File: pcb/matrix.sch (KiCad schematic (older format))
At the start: 143 parts

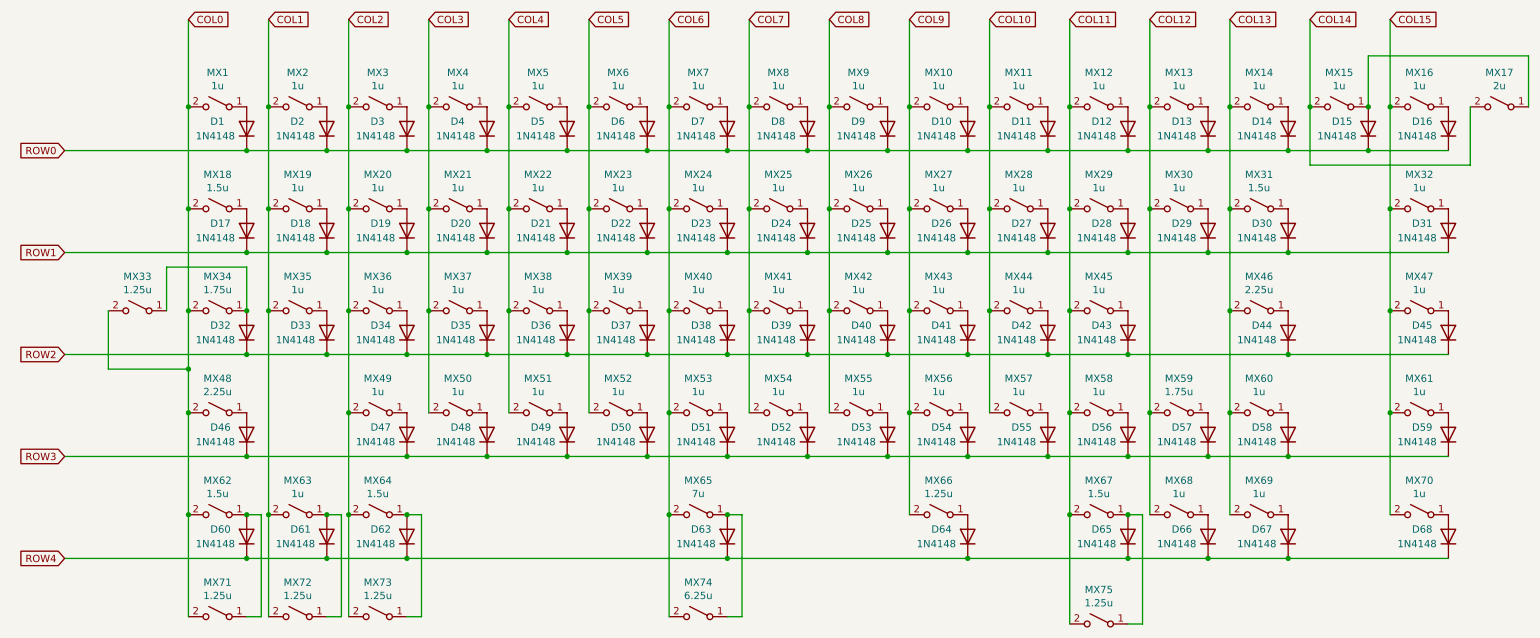
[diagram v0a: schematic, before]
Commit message: ソケットに対応。
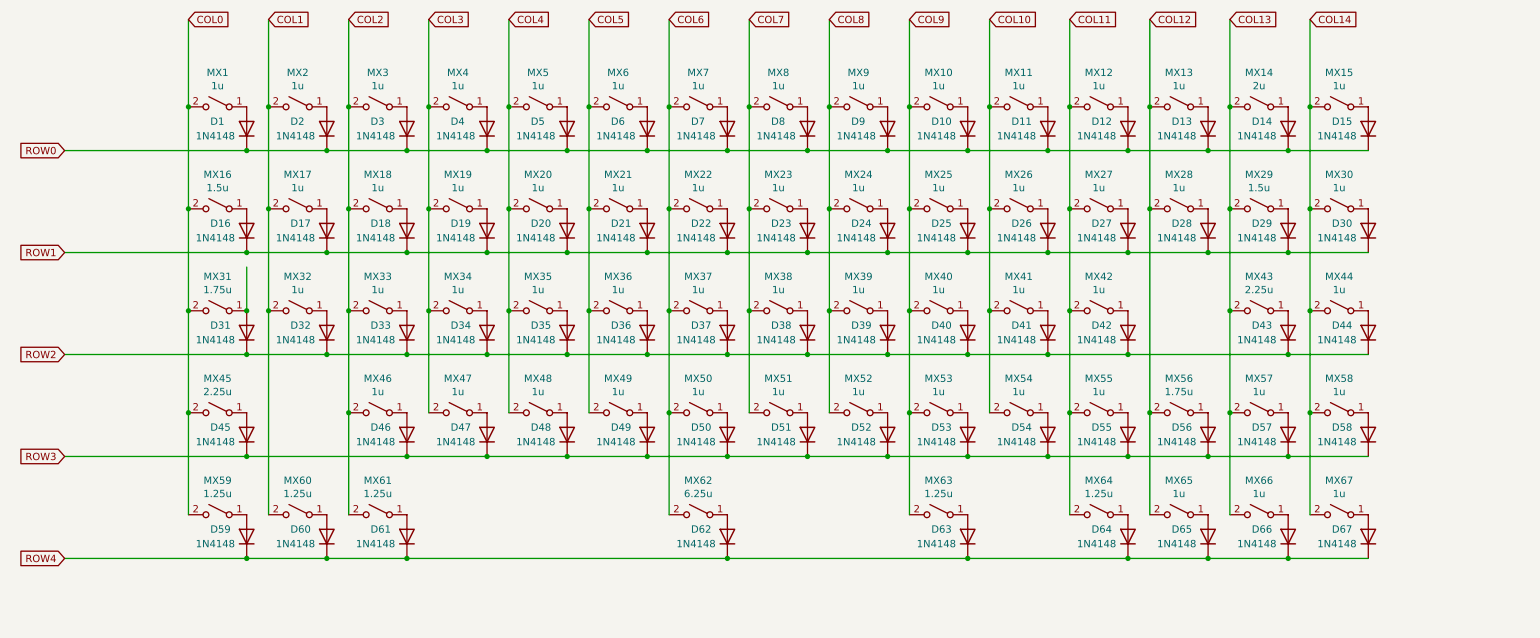
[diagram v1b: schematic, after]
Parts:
- removed D14: 1N4148, Diode_SMD:D_SOD-123, symbol Device:D
- removed MX14, MX15, MX63: 1u, MX_Only:MXOnly-1U-NoLED, symbol Switch:SW_SPST
- removed MX33: 1.25u, MX_Only:MXOnly-1.25U-NoLED, symbol Switch:SW_SPST
- removed MX62, MX64, MX67: 1.5u, MX_Only:MXOnly-1.5U-NoLED, symbol Switch:SW_SPST
- removed MX65: 7u, MX_Only:MXOnly-7U-ReversedStabilizers-NoLED, symbol Switch:SW_SPST
- MX1, MX10, MX11, MX12, MX13, MX2, MX3, MX4, MX5, MX6, MX7, MX8, MX9: footprint MX_Only:MXOnly-1U-NoLED -> MX_Only:MXOnly-1U-Hotswap
- MX14: renamed from MX17; footprint MX_Only:MXOnly-2U-NoLED -> MX_Only:MXOnly-2U-Hotswap
- MX15: renamed from MX16; footprint MX_Only:MXOnly-1U-NoLED -> MX_Only:MXOnly-1U-Hotswap
- MX16: renamed from MX18; footprint MX_Only:MXOnly-1.5U-NoLED -> MX_Only:MXOnly-1.5U-Hotswap
- MX17: renamed from MX19; footprint MX_Only:MXOnly-1U-NoLED -> MX_Only:MXOnly-1U-Hotswap
- MX18: renamed from MX20; footprint MX_Only:MXOnly-1U-NoLED -> MX_Only:MXOnly-1U-Hotswap
- MX19: renamed from MX21; footprint MX_Only:MXOnly-1U-NoLED -> MX_Only:MXOnly-1U-Hotswap
- MX20: renamed from MX22; footprint MX_Only:MXOnly-1U-NoLED -> MX_Only:MXOnly-1U-Hotswap
- MX21: renamed from MX23; footprint MX_Only:MXOnly-1U-NoLED -> MX_Only:MXOnly-1U-Hotswap
- MX22: renamed from MX24; footprint MX_Only:MXOnly-1U-NoLED -> MX_Only:MXOnly-1U-Hotswap
- MX23: renamed from MX25; footprint MX_Only:MXOnly-1U-NoLED -> MX_Only:MXOnly-1U-Hotswap
- MX24: renamed from MX26; footprint MX_Only:MXOnly-1U-NoLED -> MX_Only:MXOnly-1U-Hotswap
- MX25: renamed from MX27; footprint MX_Only:MXOnly-1U-NoLED -> MX_Only:MXOnly-1U-Hotswap
- MX26: renamed from MX28; footprint MX_Only:MXOnly-1U-NoLED -> MX_Only:MXOnly-1U-Hotswap
- MX27: renamed from MX29; footprint MX_Only:MXOnly-1U-NoLED -> MX_Only:MXOnly-1U-Hotswap
- MX28: renamed from MX30; footprint MX_Only:MXOnly-1U-NoLED -> MX_Only:MXOnly-1U-Hotswap
- MX29: renamed from MX31; footprint MX_Only:MXOnly-1.5U-NoLED -> MX_Only:MXOnly-1.5U-Hotswap
- MX30: renamed from MX32; footprint MX_Only:MXOnly-1U-NoLED -> MX_Only:MXOnly-1U-Hotswap
- MX31: renamed from MX34; footprint MX_Only:MXOnly-1.75U-NoLED -> MX_Only:MXOnly-1.75U-Hotswap
- MX32: renamed from MX35; footprint MX_Only:MXOnly-1U-NoLED -> MX_Only:MXOnly-1U-Hotswap
- MX33: renamed from MX36; footprint MX_Only:MXOnly-1U-NoLED -> MX_Only:MXOnly-1U-Hotswap
- MX34: renamed from MX37; footprint MX_Only:MXOnly-1U-NoLED -> MX_Only:MXOnly-1U-Hotswap
- MX35: renamed from MX38; footprint MX_Only:MXOnly-1U-NoLED -> MX_Only:MXOnly-1U-Hotswap
- MX36: renamed from MX39; footprint MX_Only:MXOnly-1U-NoLED -> MX_Only:MXOnly-1U-Hotswap
- MX37: renamed from MX40; footprint MX_Only:MXOnly-1U-NoLED -> MX_Only:MXOnly-1U-Hotswap
- MX38: renamed from MX41; footprint MX_Only:MXOnly-1U-NoLED -> MX_Only:MXOnly-1U-Hotswap
- MX39: renamed from MX42; footprint MX_Only:MXOnly-1U-NoLED -> MX_Only:MXOnly-1U-Hotswap
- MX40: renamed from MX43; footprint MX_Only:MXOnly-1U-NoLED -> MX_Only:MXOnly-1U-Hotswap
- MX41: renamed from MX44; footprint MX_Only:MXOnly-1U-NoLED -> MX_Only:MXOnly-1U-Hotswap
- MX42: renamed from MX45; footprint MX_Only:MXOnly-1U-NoLED -> MX_Only:MXOnly-1U-Hotswap
- MX43: renamed from MX46; footprint MX_Only:MXOnly-2.25U-NoLED -> MX_Only:MXOnly-2.25U-Hotswap
- MX44: renamed from MX47; footprint MX_Only:MXOnly-1U-NoLED -> MX_Only:MXOnly-1U-Hotswap
- MX45: renamed from MX48; footprint MX_Only:MXOnly-2.25U-NoLED -> MX_Only:MXOnly-2.25U-Hotswap
- MX46: renamed from MX49; footprint MX_Only:MXOnly-1U-NoLED -> MX_Only:MXOnly-1U-Hotswap
- MX47: renamed from MX50; footprint MX_Only:MXOnly-1U-NoLED -> MX_Only:MXOnly-1U-Hotswap
- MX48: renamed from MX51; footprint MX_Only:MXOnly-1U-NoLED -> MX_Only:MXOnly-1U-Hotswap
- MX49: renamed from MX52; footprint MX_Only:MXOnly-1U-NoLED -> MX_Only:MXOnly-1U-Hotswap
- MX50: renamed from MX53; footprint MX_Only:MXOnly-1U-NoLED -> MX_Only:MXOnly-1U-Hotswap
- MX51: renamed from MX54; footprint MX_Only:MXOnly-1U-NoLED -> MX_Only:MXOnly-1U-Hotswap
- MX52: renamed from MX55; footprint MX_Only:MXOnly-1U-NoLED -> MX_Only:MXOnly-1U-Hotswap
- MX53: renamed from MX56; footprint MX_Only:MXOnly-1U-NoLED -> MX_Only:MXOnly-1U-Hotswap
- MX54: renamed from MX57; footprint MX_Only:MXOnly-1U-NoLED -> MX_Only:MXOnly-1U-Hotswap
- MX55: renamed from MX58; footprint MX_Only:MXOnly-1U-NoLED -> MX_Only:MXOnly-1U-Hotswap
- MX56: renamed from MX59; footprint MX_Only:MXOnly-1.75U-NoLED -> MX_Only:MXOnly-1.75U-Hotswap
- MX57: renamed from MX60; footprint MX_Only:MXOnly-1U-NoLED -> MX_Only:MXOnly-1U-Hotswap
- MX58: renamed from MX61; footprint MX_Only:MXOnly-1U-NoLED -> MX_Only:MXOnly-1U-Hotswap
- MX59: renamed from MX71; footprint MX_Only:MXOnly-1.25U-NoLED -> MX_Only:MXOnly-1.25U-Hotswap
- MX60: renamed from MX72; footprint MX_Only:MXOnly-1.25U-NoLED -> MX_Only:MXOnly-1.25U-Hotswap
- MX61: renamed from MX73; footprint MX_Only:MXOnly-1.25U-NoLED -> MX_Only:MXOnly-1.25U-Hotswap
- MX62: renamed from MX74; footprint MX_Only:MXOnly-6.25U-ReversedStabilizers-NoLED -> MX_Only:MXOnly-6.25U-Hotswap-ReversedStabilizers
- MX63: renamed from MX66; footprint MX_Only:MXOnly-1.25U-NoLED -> MX_Only:MXOnly-1.25U-Hotswap
- MX64: renamed from MX75; footprint MX_Only:MXOnly-1.25U-NoLED -> MX_Only:MXOnly-1.25U-Hotswap
- MX65: renamed from MX68; footprint MX_Only:MXOnly-1U-NoLED -> MX_Only:MXOnly-1U-Hotswap
- MX66: renamed from MX69; footprint MX_Only:MXOnly-1U-NoLED -> MX_Only:MXOnly-1U-Hotswap
- MX67: renamed from MX70; footprint MX_Only:MXOnly-1U-NoLED -> MX_Only:MXOnly-1U-Hotswap
- renumbered D15 to D14, D16 to D15, D17 to D16, D18 to D17, D19 to D18, D20 to D19, D21 to D20, D22 to D21, D23 to D22, D24 to D23, D25 to D24, D26 to D25, D27 to D26, D28 to D27, D29 to D28, D30 to D29, D31 to D30, D32 to D31, D33 to D32, D34 to D33, D35 to D34, D36 to D35, D37 to D36, D38 to D37, D39 to D38, D40 to D39, D41 to D40, D42 to D41, D43 to D42, D44 to D43, D45 to D44, D46 to D45, D47 to D46, D48 to D47, D49 to D48, D50 to D49, D51 to D50, D52 to D51, D53 to D52, D54 to D53, D55 to D54, D56 to D55, D57 to D56, D58 to D57, D59 to D58, D60 to D59, D61 to D60, D62 to D61, D63 to D62, D64 to D63, D65 to D64, D66 to D65, D67 to D66, D68 to D67
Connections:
- net COL15 is gone; now on net COL14: MX15.2 (B), MX30.2 (B), MX44.2 (B), MX58.2 (B), MX67.2 (B)
- net COL13: now also MX14.2 (B)
- net COL14: no longer MX14.2 (B)
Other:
- moved on the sheet: D14, D15, D30, D44, D58, D67, MX14, MX15, MX30, MX44, MX58, MX59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
